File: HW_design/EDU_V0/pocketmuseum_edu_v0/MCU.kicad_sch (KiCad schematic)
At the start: 35 parts, among them J201 TF-015, J205 BM04B-SRSS-TB, J206 BM04B-SRSS-TB, SW201 PTS636, U201 ESP32-C6-MINI-1/U

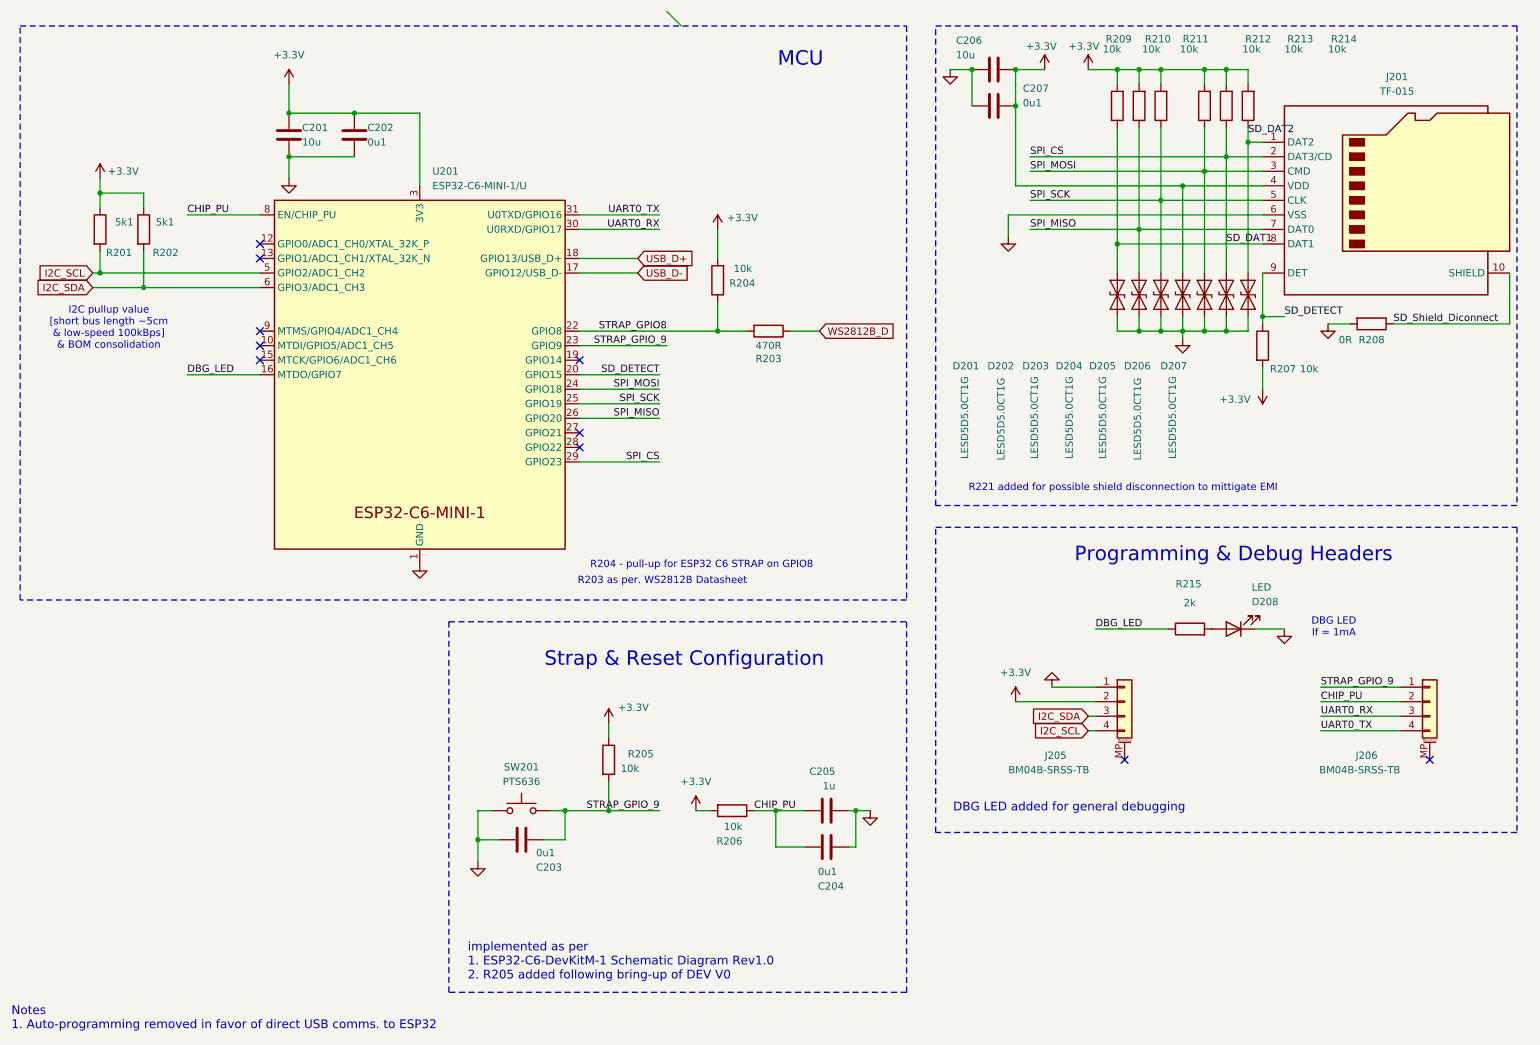
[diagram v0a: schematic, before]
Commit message: Added Mic & Light Sensor to EDU_V0
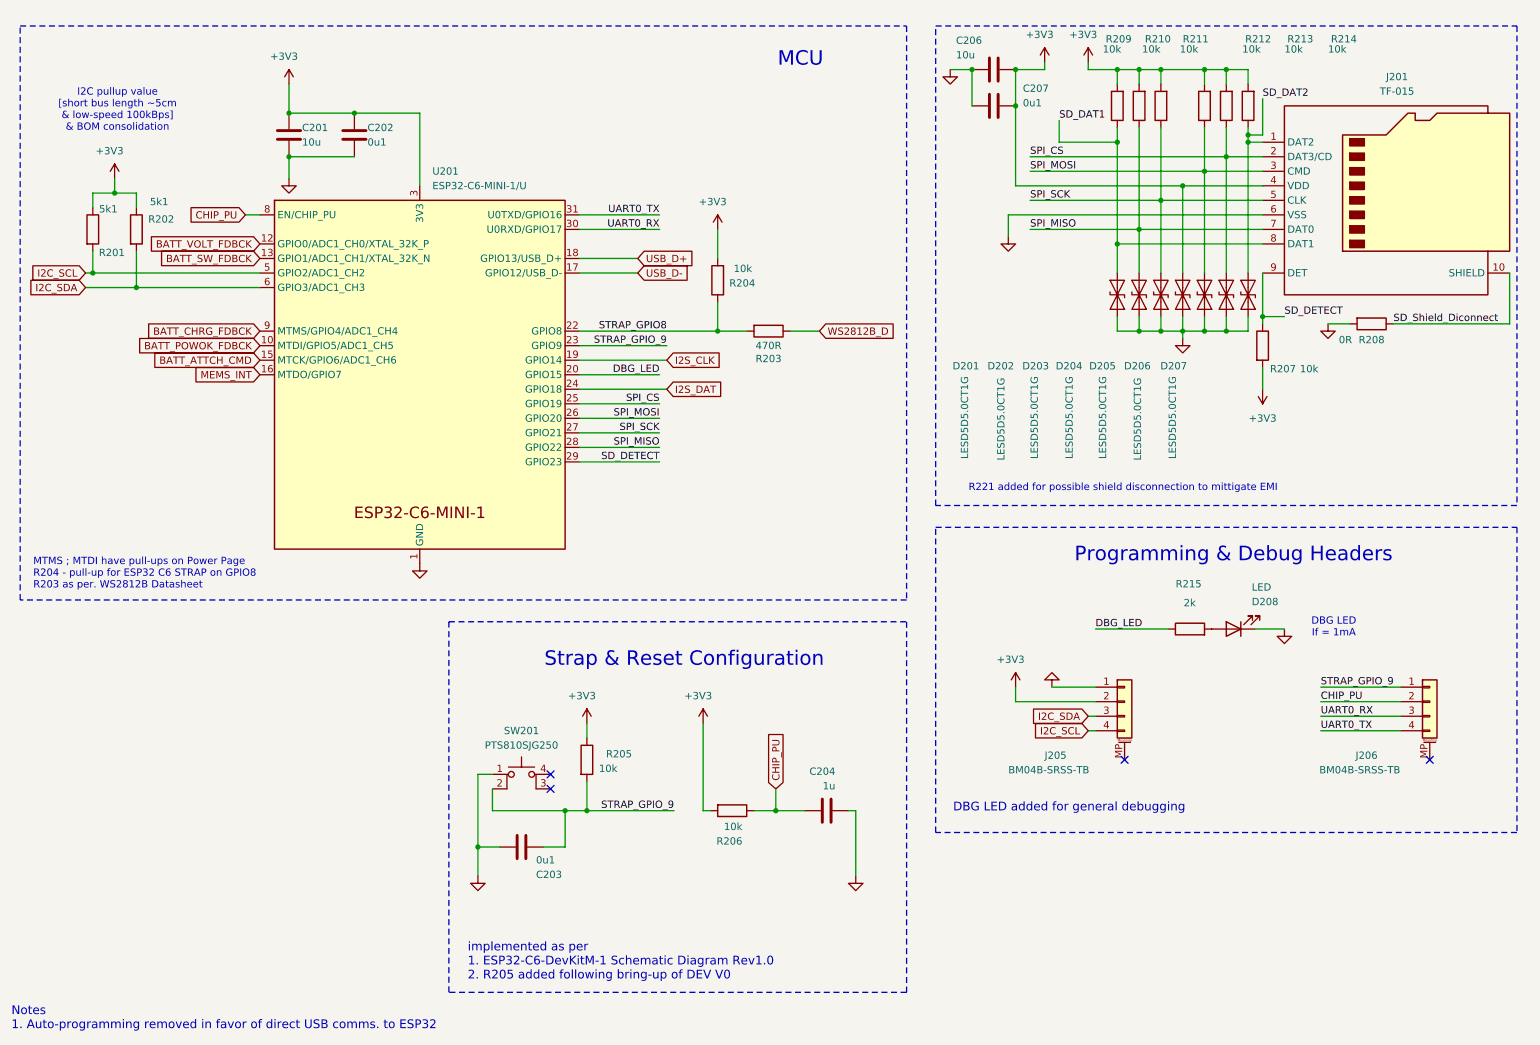
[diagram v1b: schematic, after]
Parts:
- removed C204: 0u1, Capacitor_SMD:C_0402_1005Metric, symbol Device:C
- removed SW201: PTS636, Button_Switch_SMD:SW_Tactile_SPST_NO_Straight_CK_PTS636Sx25SMTRLFS, symbol Switch:SW_Push
- added SW201: PTS810SJG250, Button_Switch_SMD:SW_SPST_PTS810, symbol Switch:SW_MEC_5E
- renumbered C205 to C204
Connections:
- net DBG_LED: now also U201.20 (GPIO15); no longer U201.16 (MTDO/GPIO7)
- net GND: now also SW201.1
- net SD_DAT1: no longer D206.1 (A1), J201.2 (DAT3/CD), R213.1, U201.29 (GPIO23)
- net SD_DETECT: now also U201.29 (GPIO23); no longer U201.20 (GPIO15)
- net SPI_MISO: now also U201.28 (GPIO22); no longer U201.26 (GPIO20)
- net SPI_MOSI: now also U201.26 (GPIO20); no longer U201.24 (GPIO18)
- net SPI_SCK: now also U201.27 (GPIO21); no longer U201.25 (GPIO19)
- net STRAP_GPIO_9: now also SW201.2
- net BATT_POWOK_FDBCK: now reaches U201.10 (MTDI/GPIO5/ADC1_CH5)
- net BATT_VOLT_FDBCK: now reaches U201.12 (GPIO0/ADC1_CH0/XTAL_32K_P)
- net BATT_SW_FDBCK: now reaches U201.13 (GPIO1/ADC1_CH1/XTAL_32K_N)
- net BATT_ATTCH_CMD: now reaches U201.15 (MTCK/GPIO6/ADC1_CH6)
- net I2S_CLK: now reaches U201.19 (GPIO14)
- net BATT_CHRG_FDBCK: now reaches U201.9 (MTMS/GPIO4/ADC1_CH4)
- net +3.3V renamed +3V3
- new net I2S_DAT: U201.24 (GPIO18)
- new net MEMS_INT: U201.16 (MTDO/GPIO7)
- new net SPI_CS: D206.1 (A1), J201.2 (DAT3/CD), R213.1, U201.25 (GPIO19)
- no-connect marks 10 -> 4
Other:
- note added: "MTMS ; MTDI have pull-ups on Power Page R204 - pull-up for ESP32 C6 STRAP on GPIO8 R203 as per. WS2812B Datasheet"
- note removed: "R203 as per. WS2812B Datasheet"
- note removed: "R204 - pull-up for ESP32 C6 STRAP on GPIO8"
- moved on the sheet: C203, R201, R202, R205

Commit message: Diagram review complete
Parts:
- removed D201, D202, D203, D204, D205, D206, D207: LESD5D5.0CT1G, Diode_SMD:D_SOD-523, symbol Diode:ESD9B5.0ST5G
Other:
- moved on the sheet: C206, C207, J201, R207, R208, R209, R210, R211, R212, R213, R214

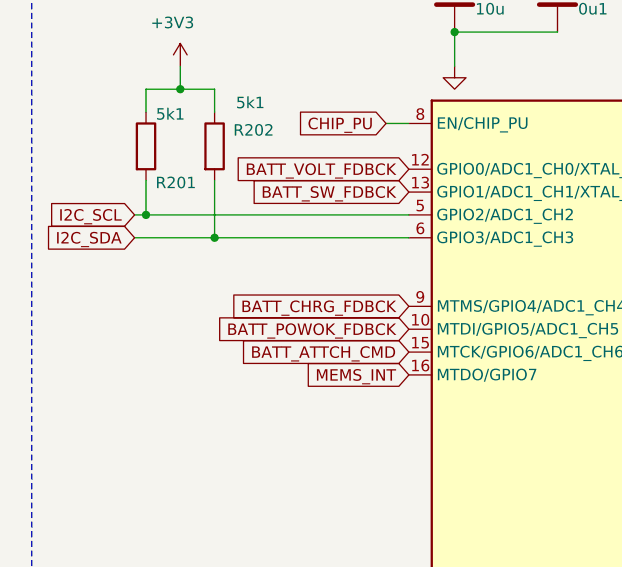
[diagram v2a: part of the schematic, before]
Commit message: EDUV0 added TP n routing in progress
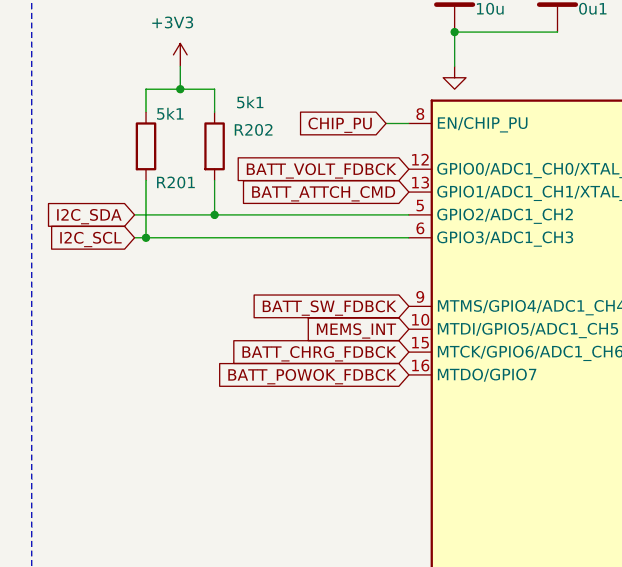
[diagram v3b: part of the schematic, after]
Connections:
- net BATT_ATTCH_CMD: now also U201.13 (GPIO1/ADC1_CH1/XTAL_32K_N); no longer U201.15 (MTCK/GPIO6/ADC1_CH6)
- net BATT_CHRG_FDBCK: now also U201.15 (MTCK/GPIO6/ADC1_CH6); no longer U201.9 (MTMS/GPIO4/ADC1_CH4)
- net BATT_POWOK_FDBCK: now also U201.16 (MTDO/GPIO7); no longer U201.10 (MTDI/GPIO5/ADC1_CH5)
- net BATT_SW_FDBCK: now also U201.9 (MTMS/GPIO4/ADC1_CH4); no longer U201.13 (GPIO1/ADC1_CH1/XTAL_32K_N)
- net I2C_SCL: now also U201.6 (GPIO3/ADC1_CH3); no longer U201.5 (GPIO2/ADC1_CH2)
- net I2C_SDA: now also U201.5 (GPIO2/ADC1_CH2); no longer U201.6 (GPIO3/ADC1_CH3)
- net MEMS_INT: now also U201.10 (MTDI/GPIO5/ADC1_CH5); no longer U201.16 (MTDO/GPIO7)
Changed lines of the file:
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@@
 	(title_block
 		(title "POCKETMUSEUM EDU V0")
-		(date "2025-08-18")
-		(rev "2")
+		(date "2025-08-21")
+		(rev "3")
 		(company "Bucharest Applied STEAM Museum")
+		(comment 1 "Flipped Batt_CMD & FB GPIOs")
 	)
 	(junction
@@
 	)
 	(junction
+		(at 39.37 62.23)
+		(diameter 0)
+		(color 0 0 0 0)
+	)
+	(junction
 		(at 236.22 76.2)
 		(diameter 0)
@@
 	)
 	(junction
-		(at 31.75 62.23)
-		(diameter 0)
-		(color 0 0 0 0)
-	)
-	(junction
 		(at 66.04 41.91)
 		(diameter 0)
@@
 	)
 	(junction
+		(at 31.75 64.77)
+		(diameter 0)
+		(color 0 0 0 0)
+	)
+	(junction
 		(at 193.04 39.37)
 		(diameter 0)
@@
 	(junction
 		(at 226.06 50.8)
-		(diameter 0)
-		(color 0 0 0 0)
-	)
-	(junction
-		(at 39.37 64.77)
 		(diameter 0)
 		(color 0 0 0 0)
@@
 	(wire
 		(pts
-			(xy 31.75 62.23) (xy 60.96 62.23)
+			(xy 30.48 62.23) (xy 39.37 62.23)
 		)
 		(stroke
@@
 	(wire
 		(pts
-			(xy 30.48 62.23) (xy 31.75 62.23)
-		)
-		(stroke
-			(width 0)
-			(type default)
-		)
-	)
-	(wire
-		(pts
 			(xy 191.77 62.23) (xy 191.77 58.42)
 		)
@@
 	(wire
 		(pts
-			(xy 31.75 58.42) (xy 31.75 62.23)
-		)
-		(stroke
-			(width 0)
-			(type default)
-		)
-	)
-	(wire
-		(pts
 			(xy 116.84 52.07) (xy 130.81 52.07)
 		)
@@
 	(wire
 		(pts
-			(xy 39.37 58.42) (xy 39.37 64.77)
-		)
-		(stroke
-			(width 0)
-			(type default)
-		)
-	)
-	(wire
-		(pts
 			(xy 226.06 43.18) (xy 226.06 50.8)
 		)
@@
 	(wire
 		(pts
+			(xy 30.48 64.77) (xy 31.75 64.77)
+		)
+		(stroke
+			(width 0)
+			(type default)
+		)
+	)
+	(wire
+		(pts
 			(xy 116.84 54.61) (xy 130.81 54.61)
 		)
@@
 	(wire
 		(pts
-			(xy 39.37 64.77) (xy 60.96 64.77)
-		)
-		(stroke
-			(width 0)
-			(type default)
-		)
-	)
-	(wire
-		(pts
 			(xy 140.97 54.61) (xy 140.97 59.69)
 		)
@@
 	(wire
 		(pts
+			(xy 31.75 64.77) (xy 60.96 64.77)
+		)
+		(stroke
+			(width 0)
+			(type default)
+		)
+	)
+	(wire
+		(pts
 			(xy 193.04 53.34) (xy 236.22 53.34)
 		)
@@
 	(wire
 		(pts
+			(xy 31.75 58.42) (xy 31.75 64.77)
+		)
+		(stroke
+			(width 0)
+			(type default)
+		)
+	)
+	(wire
+		(pts
 			(xy 114.3 162.56) (xy 114.3 156.21)
 		)
@@
 	(wire
 		(pts
-			(xy 30.48 64.77) (xy 39.37 64.77)
+			(xy 39.37 58.42) (xy 39.37 62.23)
+		)
+		(stroke
+			(width 0)
+			(type default)
+		)
+	)
+	(wire
+		(pts
+			(xy 39.37 62.23) (xy 60.96 62.23)
 		)
 		(stroke
@@
 	(global_label "BATT_POWOK_FDBCK"
 		(shape input)
-		(at 60.96 74.93 180)
+		(at 60.96 80.01 180)
 		(fields_autoplaced yes)
 		(effects
@@
 		)
 		(property "Intersheetrefs" "${INTERSHEET_REFS}"
-			(at 38.9248 74.93 0)
+			(at 38.9248 80.01 0)
 			(effects
 				(font
@@
 	(global_label "MEMS_INT"
 		(shape input)
-		(at 60.96 80.01 180)
+		(at 60.96 74.93 180)
 		(fields_autoplaced yes)
 		(effects
@@
 		)
 		(property "Intersheetrefs" "${INTERSHEET_REFS}"
-			(at 48.843 80.01 0)
+			(at 48.843 74.93 0)
 			(effects
 				(font
@@
 	(global_label "BATT_ATTCH_CMD"
 		(shape input)
-		(at 60.96 77.47 180)
+		(at 60.96 59.69 180)
 		(fields_autoplaced yes)
 		(effects
@@
 		)
 		(property "Intersheetrefs" "${INTERSHEET_REFS}"
-			(at 42.1301 77.47 0)
+			(at 42.1301 59.69 0)
 			(effects
 				(font
@@
 	(global_label "I2C_SCL"
 		(shape input)
-		(at 30.48 62.23 180)
+		(at 30.48 64.77 180)
 		(fields_autoplaced yes)
 		(effects
@@
 		)
 		(property "Intersheetrefs" "${INTERSHEET_REFS}"
-			(at 19.9353 62.23 0)
+			(at 19.9353 64.77 0)
 			(effects
 				(font
@@
 	(global_label "BATT_CHRG_FDBCK"
 		(shape input)
-		(at 60.96 72.39 180)
+		(at 60.96 77.47 180)
 		(fields_autoplaced yes)
 		(effects
@@
 		)
 		(property "Intersheetrefs" "${INTERSHEET_REFS}"
-			(at 40.4367 72.39 0)
+			(at 40.4367 77.47 0)
 			(effects
 				(font
@@
 		)
 	)
-	(global_label "BATT_SW_FDBCK"
-		(shape input)
-		(at 60.96 59.69 180)
-		(fields_autoplaced yes)
-		(effects
-			(font
-				(size 1.27 1.27)
-			)
-			(justify right)
-		)
-		(property "Intersheetrefs" "${INTERSHEET_REFS}"
-			(at 42.9163 59.69 0)
-			(effects
-				(font
-					(size 1.27 1.27)
-				)
-				(justify right)
-				(hide yes)
-			)
-		)
-	)
 	(global_label "I2S_CLK"
 		(shape input)
@@
 	(global_label "I2C_SDA"
 		(shape input)
-		(at 30.48 64.77 180)
+		(at 30.48 62.23 180)
 		(fields_autoplaced yes)
 		(effects
@@
 		)
 		(property "Intersheetrefs" "${INTERSHEET_REFS}"
-			(at 19.8748 64.77 0)
+			(at 19.8748 62.23 0)
 			(effects
 				(font
+					(size 1.27 1.27)
+				)
+				(justify right)
+				(hide yes)
+			)
+		)
+	)
+	(global_label "BATT_SW_FDBCK"
+		(shape input)
+		(at 60.96 72.39 180)
+		(fields_autoplaced yes)
+		(effects
+			(font
+				(size 1.27 1.27)
+			)
+			(justify right)
+		)
+		(property "Intersheetrefs" "${INTERSHEET_REFS}"
+			(at 42.9163 72.39 0)
+			(effects
+				(font

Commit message: EDUV0 Production Files
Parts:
- J205, J206: value BM04B-SRSS-TB -> SM04B-SRSS-TB
- R215: value 2k -> 1k2
